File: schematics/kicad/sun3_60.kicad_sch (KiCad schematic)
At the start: 0 parts

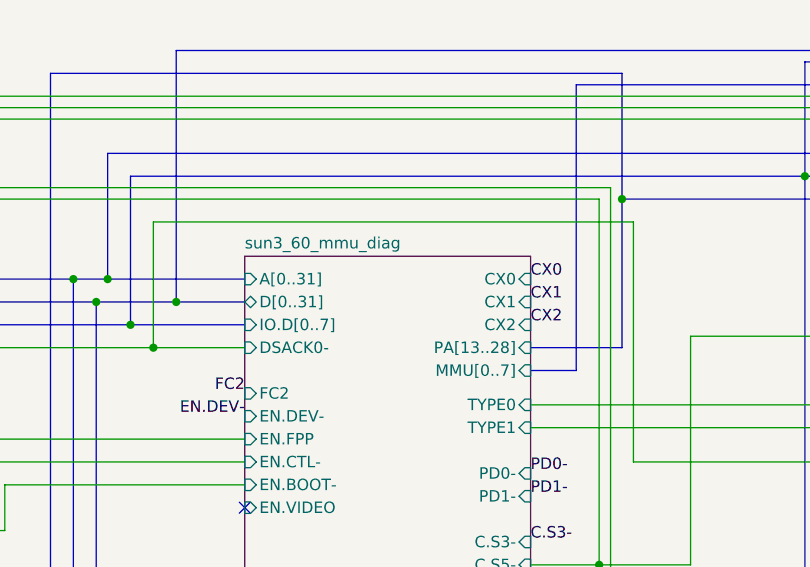
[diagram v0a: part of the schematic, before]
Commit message: First draft for an expanded MMU
This version uses vintage parts except for the SRAM, which are IS61C5128AS-25HLI (they could be QLI instead)
Unfortunately, this requires:
* 2 more 74ALS245 to buffer the second byte of PMAP indices in the SMAP
* one more LS2518 (!) to extend the context register
* a couple of 74CBTLV3257 to be able to stay in "normal" Sun3 mode with minimal delays on the signals
* a couple of switches to enabled/disable the new features
* some extra passives
* U231, a PAL16L8, needs another input and another two outputs, or can be split in two PALs (or GAL, CPLDs, ...)

Also this does not include tne necessary decoupling on the new components
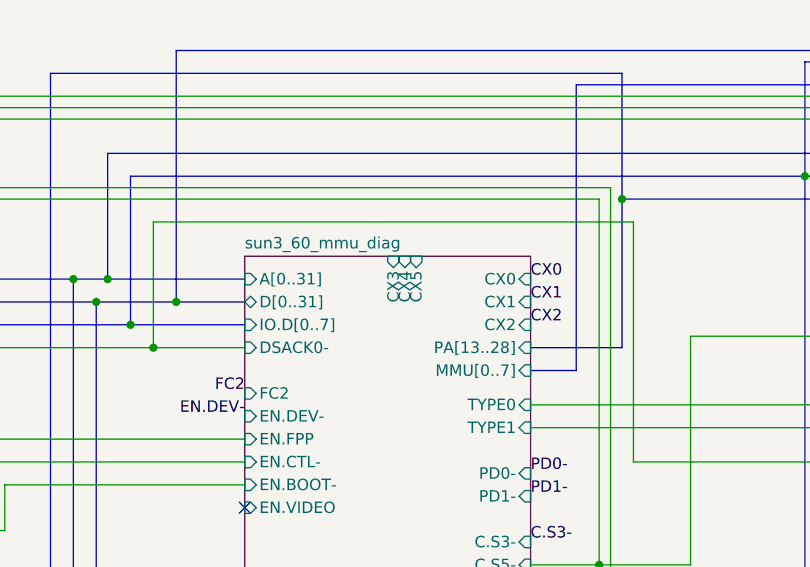
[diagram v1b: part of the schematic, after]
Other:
- sheet sun3_60_mmu_diag ports: added CX3, CX4, CX5; removed none
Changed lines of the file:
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@@
 (kicad_sch
-	(version 20231120)
+	(version 20250114)
 	(generator "eeschema")
-	(generator_version "8.0")
+	(generator_version "9.0")
 	(paper "A4")
 	(title_block
@@
 		(at 29.21 36.83)
 		(size 29.21 105.41)
+		(exclude_from_sim no)
+		(in_bom yes)
+		(on_board yes)
+		(dnp no)
 		(fields_autoplaced yes)
 		(stroke
@@
 		(at 99.06 36.83)
 		(size 31.75 57.15)
+		(exclude_from_sim no)
+		(in_bom yes)
+		(on_board yes)
+		(dnp no)
 		(fields_autoplaced yes)
 		(stroke
@@
 			)
 		)
-		(pin "MMU[0..7]" input
-			(at 130.81 49.53 0)
-			(effects
-				(font
-					(size 1.27 1.27)
-				)
-				(justify right)
-			)
-		)
 		(pin "READ-" input
 			(at 130.81 80.01 0)
@@
 			)
 		)
+		(pin "CX3" input
+			(at 115.57 36.83 90)
+			(effects
+				(font
+					(size 1.27 1.27)
+				)
+				(justify right)
+			)
+		)
+		(pin "CX4" input
+			(at 116.84 36.83 90)
+			(effects
+				(font
+					(size 1.27 1.27)
+				)
+				(justify right)
+			)
+		)
+		(pin "CX5" input
+			(at 118.11 36.83 90)
+			(effects
+				(font
+					(size 1.27 1.27)
+				)
+				(justify right)
+			)
+		)
+		(pin "MMU[0..7]" input
+			(at 130.81 49.53 0)
+			(effects
+				(font
+					(size 1.27 1.27)
+				)
+				(justify right)
+			)
+		)
 		(instances
 			(project "sun3_60"
@@
 		(at 173.99 22.86)
 		(size 30.48 109.22)
+		(exclude_from_sim no)
+		(in_bom yes)
+		(on_board yes)
+		(dnp no)
 		(fields_autoplaced yes)
 		(stroke
@@
 		(at 119.38 127)
 		(size 24.13 60.96)
+		(exclude_from_sim no)
+		(in_bom yes)
+		(on_board yes)
+		(dnp no)
 		(fields_autoplaced yes)
 		(stroke
@@
 		(at 143.51 87.63)
 		(size 15.24 27.94)
+		(exclude_from_sim no)
+		(in_bom yes)
+		(on_board yes)
+		(dnp no)
 		(fields_autoplaced yes)
 		(stroke
@@
 		(at 82.55 124.46)
 		(size 26.67 67.31)
+		(exclude_from_sim no)
+		(in_bom yes)
+		(on_board yes)
+		(dnp no)
 		(fields_autoplaced yes)
 		(stroke
@@
 		(at 33.02 149.86)
 		(size 20.32 44.45)
+		(exclude_from_sim no)
+		(in_bom yes)
+		(on_board yes)
+		(dnp no)
 		(fields_autoplaced yes)
 		(stroke
@@
 		(at 231.14 12.7)
 		(size 25.4 52.07)
+		(exclude_from_sim no)
+		(in_bom yes)
+		(on_board yes)
+		(dnp no)
 		(fields_autoplaced yes)
 		(stroke
@@
 			)
 		)
-		(pin "MMU[0..7]" input
-			(at 231.14 33.02 180)
-			(effects
-				(font
-					(size 1.27 1.27)
-				)
-				(justify left)
-			)
-		)
 		(pin "SCC.IRQ-" input
 			(at 256.54 62.23 0)
@@
 			)
 		)
+		(pin "MMU[0..7]" input
+			(at 231.14 33.02 180)
+			(effects
+				(font
+					(size 1.27 1.27)
+				)
+				(justify left)
+			)
+		)
 		(instances
 			(project "sun3_60"
@@
 		(at 231.14 71.12)
 		(size 21.59 49.53)
+		(exclude_from_sim no)
+		(in_bom yes)
+		(on_board yes)
+		(dnp no)
 		(fields_autoplaced yes)
 		(stroke
@@
 		)
 	)
+	(embedded_fonts no)
 )

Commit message: cleanup (?)
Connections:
- no-connect marks 31 -> 35
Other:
- sheet sun3_60_mmu_diag ports: added PA[29..36]; removed none
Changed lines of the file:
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@@
 	)
 	(no_connect
+		(at 115.57 36.83)
+	)
+	(no_connect
 		(at 109.22 179.07)
 	)
@@
 	)
 	(no_connect
+		(at 116.84 36.83)
+	)
+	(no_connect
 		(at 109.22 149.86)
 	)
@@
 	)
 	(no_connect
+		(at 114.3 36.83)
+	)
+	(no_connect
+		(at 118.11 36.83)
+	)
+	(no_connect
 		(at 204.47 52.07)
 	)
@@
 			(effects
 				(font
+					(size 1.27 1.27)
+				)
+				(justify right)
+			)
+		)
+		(pin "PA[29..36]" bidirectional
+			(at 114.3 36.83 90)
+			(effects
+				(font

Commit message: draft, ugly and WiP
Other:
- added sheet SIMMs 2 (sun3_60_simm1.kicad_sch)
- sheet S8A Memory ports: added none; removed PA22/02
- sheet SCSI 2, Parity ports: added RD_PARX-, WR_PARX-; removed RD.PAR0-, RD.PAR4-, RD.PAR5-, RD.PAR6-, RD.PAR7-, WR.PAR0-, WR.PAR4-
- sheet SIMMs 1 ports: added none; removed PA22/02
- sheet sun3_60_cpu ports: added FC0, FC1; removed none
- sheet sun3_60_eeprom ports: added AS, C.S3, C.S5, C.S7, D[0..31], RD_PARX-, WR.DIAG-, WR_PARX-; removed RD.PAR0-, RD.PAR4-, RD.PAR5-, RD.PAR6-, RD.PAR7-, WR.PAR0-, WR.PAR4-
- sheet sun3_60_mmu_diag ports: added AS, DIS.RAS-, DS-, EN.UART-, FC0, FC1, OE.BOOT-, R.ACK-, WR.DIAG-; removed none

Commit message: update
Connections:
- no-connect marks 35 -> 42
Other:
- sheet sun3_60_eeprom ports: added BERR.T-, HALT-, POR-, RD.PAR0-, RD.PAR4-, RD.PAR5-, RD.PAR6-, RD.PAR7-, WDOG-, WR.PAR0-, WR.PAR4-; removed none
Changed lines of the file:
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@@
 	)
 	(no_connect
+		(at 173.99 113.03)
+	)
+	(no_connect
 		(at 58.42 99.06)
 	)
 	(no_connect
+		(at 173.99 116.84)
+	)
+	(no_connect
 		(at 95.25 191.77)
 	)
@@
 	)
 	(no_connect
+		(at 173.99 115.57)
+	)
+	(no_connect
 		(at 109.22 144.78)
 	)
@@
 	)
 	(no_connect
+		(at 173.99 119.38)
+	)
+	(no_connect
 		(at 204.47 54.61)
 	)
@@
 	)
 	(no_connect
+		(at 173.99 120.65)
+	)
+	(no_connect
 		(at 82.55 162.56)
 	)
@@
 	)
 	(no_connect
+		(at 173.99 114.3)
+	)
+	(no_connect
 		(at 204.47 52.07)
 	)
@@
 	)
 	(no_connect
+		(at 173.99 118.11)
+	)
+	(no_connect
 		(at 204.47 59.69)
 	)
@@
 		)
 	)
+	(label "BERR.T-"
+		(at 62.23 125.73 0)
+		(effects
+			(font
+				(size 1.27 1.27)
+			)
+			(justify left bottom)
+		)
+	)
 	(label "D[0..31]"
 		(at 63.5 41.91 0)
@@
 		)
 	)
+	(label "WDOG-"
+		(at 204.47 107.95 0)
+		(effects
+			(font
+				(size 1.27 1.27)
+			)
+			(justify left bottom)
+		)
+	)
 	(label "R.ACK-"
 		(at 58.42 92.71 0)
@@
 		)
 	)
+	(label "BERR.T-"
+		(at 204.47 119.38 0)
+		(effects
+			(font
+				(size 1.27 1.27)
+			)
+			(justify left bottom)
+		)
+	)
 	(label "PU2"
 		(at 29.21 132.08 180)
@@
 		)
 	)
+	(label "POR-"
+		(at 204.47 110.49 0)
+		(effects
+			(font
+				(size 1.27 1.27)
+			)
+			(justify left bottom)
+		)
+	)
 	(label "C.S3"
 		(at 182.88 132.08 270)
@@
 		)
 	)
+	(label "HALT-"
+		(at 204.47 105.41 0)
+		(effects
+			(font
+				(size 1.27 1.27)
+			)
+			(justify left bottom)
+		)
+	)
 	(label "PU1"
 		(at 29.21 129.54 180)
@@
 			)
 		)
+		(pin "POR-" input
+			(at 204.47 110.49 0)
+			(effects
+				(font
+					(size 1.27 1.27)
+				)
+				(justify right)
+			)
+		)
+		(pin "RD.PAR0-" input
+			(at 173.99 113.03 180)
+			(effects
+				(font
+					(size 1.27 1.27)
+				)
+				(justify left)
+			)
+		)
+		(pin "RD.PAR4-" input
+			(at 173.99 114.3 180)
+			(effects
+				(font
+					(size 1.27 1.27)
+				)
+				(justify left)
+			)
+		)
+		(pin "RD.PAR5-" input
+			(at 173.99 115.57 180)
+			(effects
+				(font
+					(size 1.27 1.27)
+				)
+				(justify left)
+			)
+		)
+		(pin "RD.PAR6-" input
+			(at 173.99 116.84 180)
+			(effects
+				(font
+					(size 1.27 1.27)
+				)
+				(justify left)
+			)
+		)
+		(pin "RD.PAR7-" input
+			(at 173.99 118.11 180)
+			(effects
+				(font
+					(size 1.27 1.27)
+				)
+				(justify left)
+			)
+		)
+		(pin "WDOG-" output
+			(at 204.47 107.95 0)
+			(effects
+				(font
+					(size 1.27 1.27)
+				)
+				(justify right)
+			)
+		)
+		(pin "WR.PAR0-" input
+			(at 173.99 119.38 180)
+			(effects
+				(font
+					(size 1.27 1.27)
+				)
+				(justify left)
+			)
+		)
+		(pin "WR.PAR4-" input
+			(at 173.99 120.65 180)
+			(effects
+				(font
+					(size 1.27 1.27)
+				)
+				(justify left)
+			)
+		)
+		(pin "HALT-" input
+			(at 204.47 105.41 0)
+			(effects
+				(font
+					(size 1.27 1.27)
+				)
+				(justify right)
+			)
+		)
+		(pin "BERR.T-" input
+			(at 204.47 119.38 0)
+			(effects
+				(font
+					(size 1.27 1.27)
+				)
+				(justify right)
+			)
+		)
